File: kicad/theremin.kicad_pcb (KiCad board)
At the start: 2 copper layers, 146 x 91 mm, 47 parts, among them J1 Eurorack Mono Jack, J3 Expression Attachment, SW1 SW_SPDT, U1 4069, U2 4069, U3 LM386, U4 LP2950-5.0_TO92

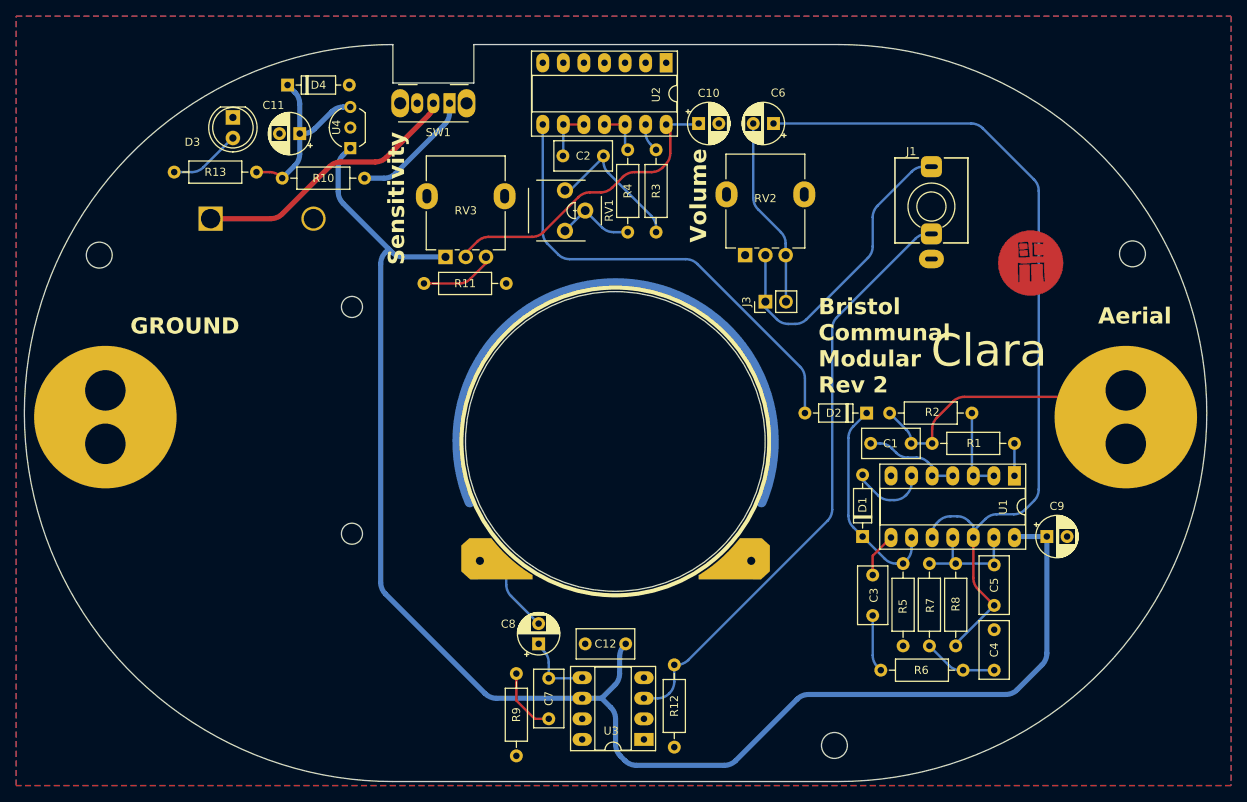
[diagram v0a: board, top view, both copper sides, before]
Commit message: Final tweaks to make sure the front plate holes are on grid
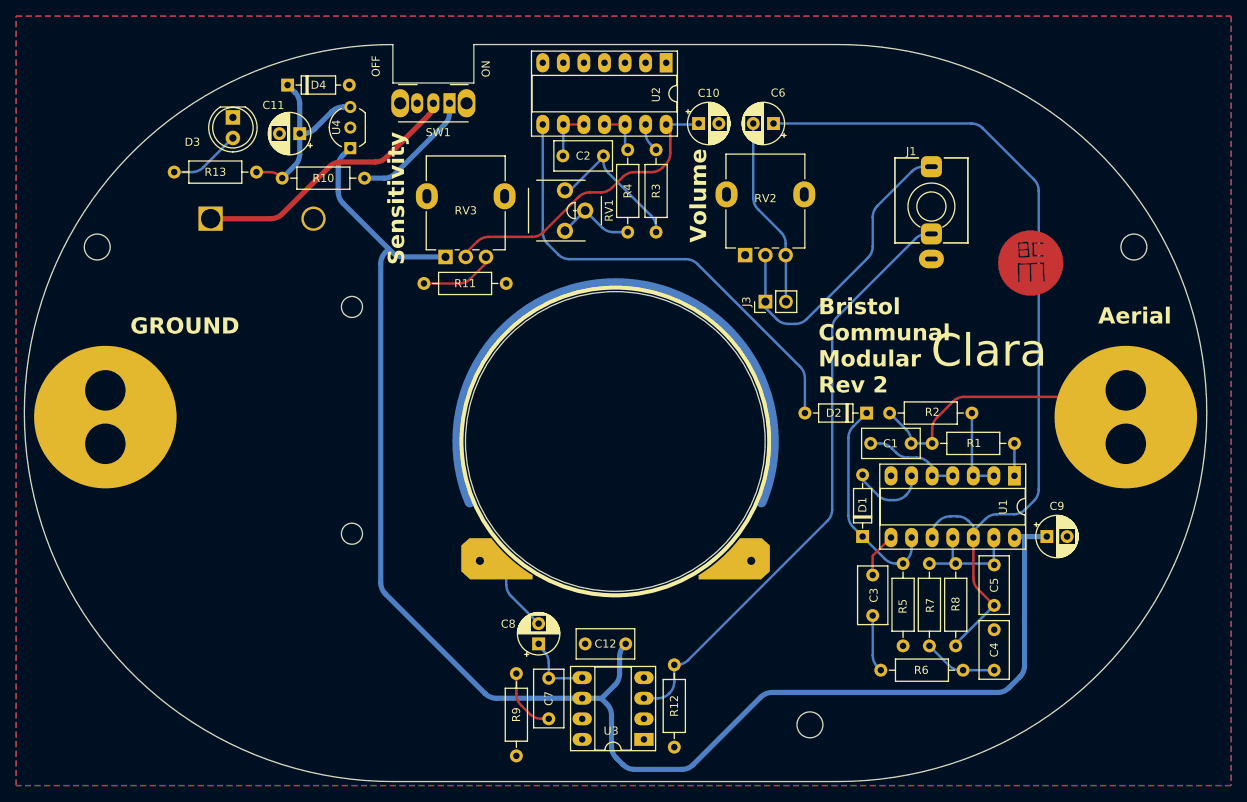
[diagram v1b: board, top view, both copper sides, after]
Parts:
- moved EF** 3.95 mm to (174.0, 135.0)
- moved EF** 1.03 mm to (86.0, 76.0)
- moved EF** 0.86 mm to (214.0, 76.0)
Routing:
- net VCC: track 190.8 -> 189.8 mm
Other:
- board text added: "OFF"
- board text added: "ON"
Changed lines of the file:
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@@
 	(footprint "MountingHole:MountingHole_3.2mm_M3"
 		(layer "F.Cu")
-		(at 86.25 77)
+		(at 86 76)
 		(descr "Mounting Hole 3.2mm, no annular, M3")
 		(tags "mounting hole 3.2mm no annular m3")
@@
 	(footprint "MountingHole:MountingHole_3.2mm_M3"
 		(layer "F.Cu")
-		(at 177.024 137.5454)
+		(at 174 135)
 		(descr "Mounting Hole 3.2mm, no annular, M3")
 		(tags "mounting hole 3.2mm no annular m3")
@@
 	(footprint "MountingHole:MountingHole_3.2mm_M3"
 		(layer "F.Cu")
-		(at 213.824 76.8454)
+		(at 214 76)
 		(descr "Mounting Hole 3.2mm, no annular, M3")
 		(tags "mounting hole 3.2mm no annular m3")
@@
 		)
 	)
+	(gr_text "ON"
+		(at 134 54 90)
+		(layer "F.SilkS")
+		(effects
+			(font
+				(size 1 1)
+				(thickness 0.15)
+			)
+		)
+	)
+	(gr_text "OFF"
+		(at 121 55 90)
+		(layer "F.SilkS")
+		(effects
+			(font
+				(size 1 1)
+				(thickness 0.15)
+			)
+			(justify left bottom)
+		)
+	)
 	(gr_text "Clara"
 		(at 188.94 91.14 0)
@@
 	(segment
 		(start 137.75 128.67)
-		(end 137.75 132)
+		(end 137.75 131.171573)
 		(width 0.3048)
 		(layer "F.Cu")
@@
 	)
 	(segment
-		(start 137.75 132)
-		(end 140 134.25)
+		(start 138.335787 132.585787)
+		(end 139.414214 133.664214)
 		(width 0.3048)
 		(layer "F.Cu")
@@
 	)
 	(segment
-		(start 140 134.25)
+		(start 140.828427 134.25)
 		(end 141.75 134.25)
 		(width 0.3048)
@@
 		(net 11)
 	)
+	(arc
+		(start 137.75 131.171573)
+		(mid 137.902241 131.93694)
+		(end 138.335787 132.585787)
+		(width 0.3048)
+		(layer "F.Cu")
+		(net 11)
+	)
+	(arc
+		(start 139.414214 133.664214)
+		(mid 140.06306 134.097759)
+		(end 140.828427 134.25)
+		(width 0.3048)
+		(layer "F.Cu")
+		(net 11)
+	)
 	(segment
 		(start 140.5 125.25)
@@
 	)
 	(segment
+		(start 152.328427 140.5)
+		(end 158.171573 140.5)
+		(width 0.635)
+		(layer "B.Cu")
+		(net 14)
+	)
+	(segment
 		(start 121.585787 76.664213)
 		(end 122 76.25)
@@
 	)
 	(segment
-		(start 203.25 126.171573)
-		(end 203.25 111.75)
+		(start 148.28 131.78)
+		(end 148.914214 132.414214)
 		(width 0.635)
 		(layer "B.Cu")
@@
 	)
 	(segment
-		(start 115.75 66.078427)
-		(end 115.75 69.171573)
+		(start 200.5 111.75)
+		(end 199.37 111.75)
 		(width 0.635)
 		(layer "B.Cu")
@@
 	)
 	(segment
-		(start 151.085787 125.164213)
-		(end 151.25 125)
+		(start 148.28 131.72)
+		(end 148.28 131.78)
 		(width 0.635)
 		(layer "B.Cu")
@@
 	)
 	(segment
-		(start 117.25 63.79)
-		(end 117.21 63.79)
+		(start 203.25 111.75)
+		(end 200.5 111.75)
 		(width 0.635)
 		(layer "B.Cu")
@@
 	)
 	(segment
-		(start 148.28 131.72)
-		(end 149.914214 130.085786)
+		(start 149.5 133.828427)
+		(end 149.5 137.671573)
 		(width 0.635)
 		(layer "B.Cu")
@@
 	)
 	(segment
-		(start 150.5 128.671573)
-		(end 150.5 126.578427)
+		(start 169.328427 131)
+		(end 197.171573 131)
 		(width 0.635)
 		(layer "B.Cu")
@@
 	)
 	(segment
-		(start 173.828427 131.25)
-		(end 198.171573 131.25)
+		(start 115.75 66.078427)
+		(end 115.75 69.171573)
 		(width 0.635)
 		(layer "B.Cu")
@@
 	)
 	(segment
-		(start 150.585787 138.835787)
-		(end 151.164214 139.414214)
+		(start 151.085787 125.164213)
+		(end 151.25 125)
 		(width 0.635)
 		(layer "B.Cu")
@@
 	)
 	(segment
-		(start 199.37 111.75)
-		(end 199.25 111.87)
+		(start 117.25 63.79)
+		(end 117.21 63.79)
 		(width 0.635)
 		(layer "B.Cu")
@@
 	)
 	(segment
-		(start 199.585787 130.664213)
-		(end 202.664214 127.585786)
+		(start 148.28 131.72)
+		(end 149.914214 130.085786)
 		(width 0.635)
 		(layer "B.Cu")
@@
 	)
 	(segment
-		(start 164.835787 139.414213)
-		(end 172.414214 131.835786)
+		(start 150.085787 139.085787)
+		(end 150.914214 139.914214)
 		(width 0.635)
 		(layer "B.Cu")
@@
 	)
 	(segment
-		(start 150 134.268427)
-		(end 150 137.421573)
+		(start 150.5 128.671573)
+		(end 150.5 126.578427)
 		(width 0.635)
 		(layer "B.Cu")
@@
 	)
 	(segment
-		(start 122 76.25)
-		(end 122.389214 76.639214)
+		(start 199.37 111.75)
+		(end 199.25 111.87)
 		(width 0.635)
 		(layer "B.Cu")
@@
 	)
 	(segment
-		(start 148.28 131.72)
-		(end 149.414214 132.854214)
+		(start 122 76.25)
+		(end 122.389214 76.639214)
 		(width 0.635)
 		(layer "B.Cu")
@@
 	)
 	(segment
+		(start 198.585787 130.414213)
+		(end 199.914214 129.085786)
+		(width 0.635)
+		(layer "B.Cu")
+		(net 14)
+	)
+	(segment
+		(start 200.5 127.671573)
+		(end 200.5 111.75)
+		(width 0.635)
+		(layer "B.Cu")
+		(net 14)
+	)
+	(segment
 		(start 121 78.078427)
 		(end 121 117.421573)
@@
 	)
 	(segment
-		(start 203.25 111.75)
-		(end 199.37 111.75)
+		(start 116.335787 70.585787)
+		(end 122 76.25)
 		(width 0.635)
 		(layer "B.Cu")
@@
 	)
 	(segment
-		(start 116.335787 70.585787)
-		(end 122 76.25)
+		(start 159.585787 139.914213)
+		(end 167.914214 131.585786)
 		(width 0.635)
 		(layer "B.Cu")
 		(net 14)
 	)
-	(segment
-		(start 152.578427 140)
-		(end 163.421573 140)
+	(arc
+		(start 149.5 137.671573)
+		(mid 149.652241 138.43694)
+		(end 150.085787 139.085787)
 		(width 0.635)
 		(layer "B.Cu")
@@
 	)
 	(arc
+		(start 152.328427 140.5)
+		(mid 151.56306 140.347759)
+		(end 150.914214 139.914214)
+		(width 0.635)
+		(layer "B.Cu")
+		(net 14)
+	)
+	(arc
 		(start 121 78.078427)
 		(mid 121.152241 77.31306)
@@
 	)
 	(arc
-		(start 198.171573 131.25)
-		(mid 198.93694 131.097759)
-		(end 199.585787 130.664213)
+		(start 149.5 133.828427)
+		(mid 149.347759 133.06306)
+		(end 148.914214 132.414214)
 		(width 0.635)
 		(layer "B.Cu")
@@
 	)
 	(arc
-		(start 202.664214 127.585786)
-		(mid 203.097759 126.93694)
-		(end 203.25 126.171573)
+		(start 167.914214 131.585786)
+		(mid 168.56306 131.152241)
+		(end 169.328427 131)
 		(width 0.635)
 		(layer "B.Cu")
@@
 	)
 	(arc
-		(start 173.828427 131.25)
-		(mid 173.06306 131.402241)
-		(end 172.414214 131.835786)
-		(width 0.635)
-		(layer "B.Cu")
-		(net 14)
-	)
-	(arc
-		(start 152.578427 140)
-		(mid 151.81306 139.847759)
-		(end 151.164214 139.414214)
+		(start 159.585787 139.914213)
+		(mid 158.93694 140.347759)
+		(end 158.171573 140.5)
 		(width 0.635)
 		(layer "B.Cu")
@@
 	)
 	(arc
-		(start 150 137.421573)
-		(mid 150.152241 138.18694)
-		(end 150.585787 138.835787)
+		(start 200.5 127.671573)
+		(mid 200.347759 128.43694)
+		(end 199.914214 129.085786)
 		(width 0.635)
 		(layer "B.Cu")
@@
 	)
 	(arc
-		(start 150 134.268427)
-		(mid 149.847759 133.50306)
-		(end 149.414214 132.854214)
-		(width 0.635)
-		(layer "B.Cu")
-		(net 14)
-	)
-	(arc
-		(start 163.421573 140)
-		(mid 164.18694 139.847759)
-		(end 164.835787 139.414213)
+		(start 133.884214 131.134214)
+		(mid 134.53306 131.567759)
+		(end 135.298427 131.72)
 		(width 0.635)
 		(layer "B.Cu")
@@
 	)
 	(arc
-		(start 133.884214 131.134214)
-		(mid 134.53306 131.567759)
-		(end 135.298427 131.72)
+		(start 197.171573 131)
+		(mid 197.93694 130.847759)
+		(end 198.585787 130.414213)
 		(width 0.635)
 		(layer "B.Cu")

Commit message: Fixing issues with layout
* Making sure speaker fixing copper isn't covered on speaker footprint
* Adding two more plated holes to make fixing speaker easier
* Making holes for battery holder smaller so easier to solder
* Adding another mounting hole for faceplate
* Tweaking value and reference text placements
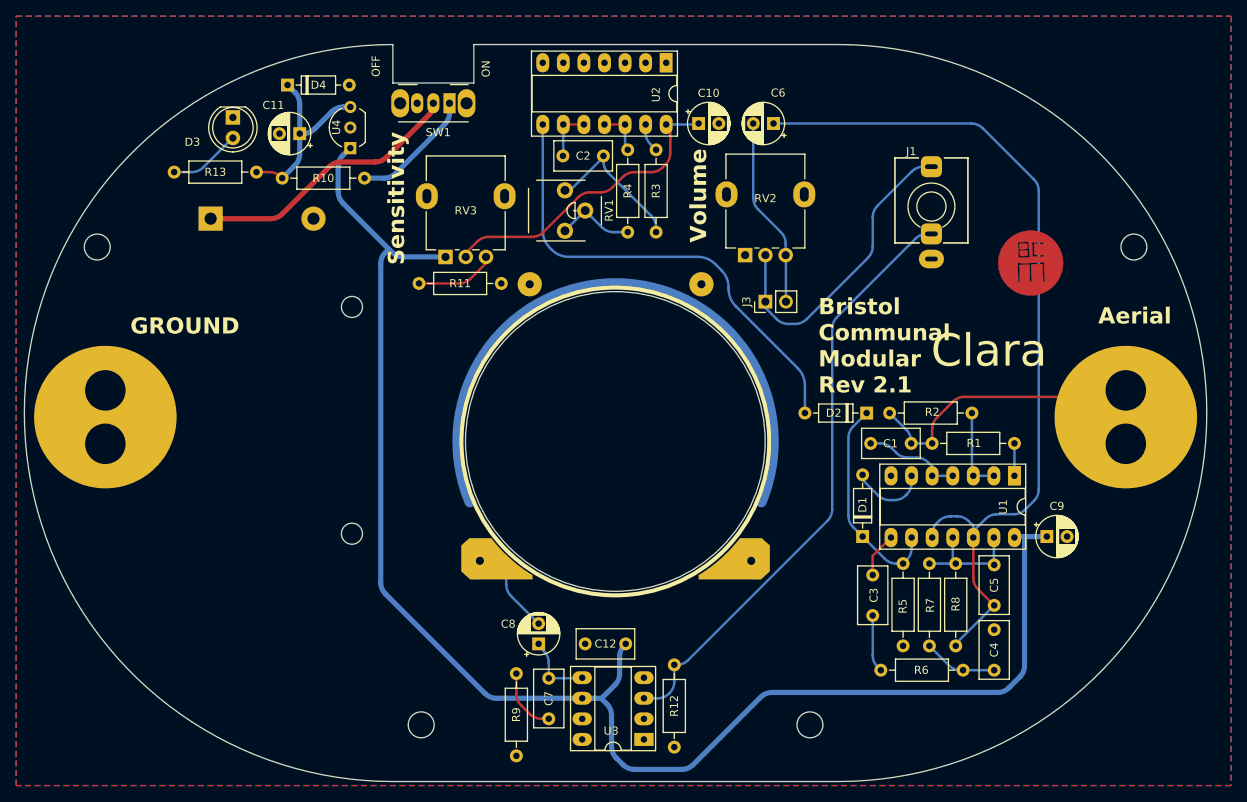
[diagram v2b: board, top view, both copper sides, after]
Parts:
- added EF**: MountingHole_3.2mm_M3, MountingHole:MountingHole_3.2mm_M3, F.Cu at (126.0, 135.0)
- RV1: footprint project-footprints:Potentiometer_THT_Bourns_3306P_Vertical -> Rumblesan_Potentiometer_THT:Potentiometer_THT_Bourns_3306P_Vertical
- moved R11 0.61 mm to (135.9, 80.5)
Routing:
- net Net-(D2-A): track 58.0 -> 59.0 mm
- net Net-(R11-Pad2): track 9.32 -> 9.98 mm
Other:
- board text added: "Bristol Communal Modular Rev 2.1"
- board text removed: "Bristol Communal Modular Rev 2"

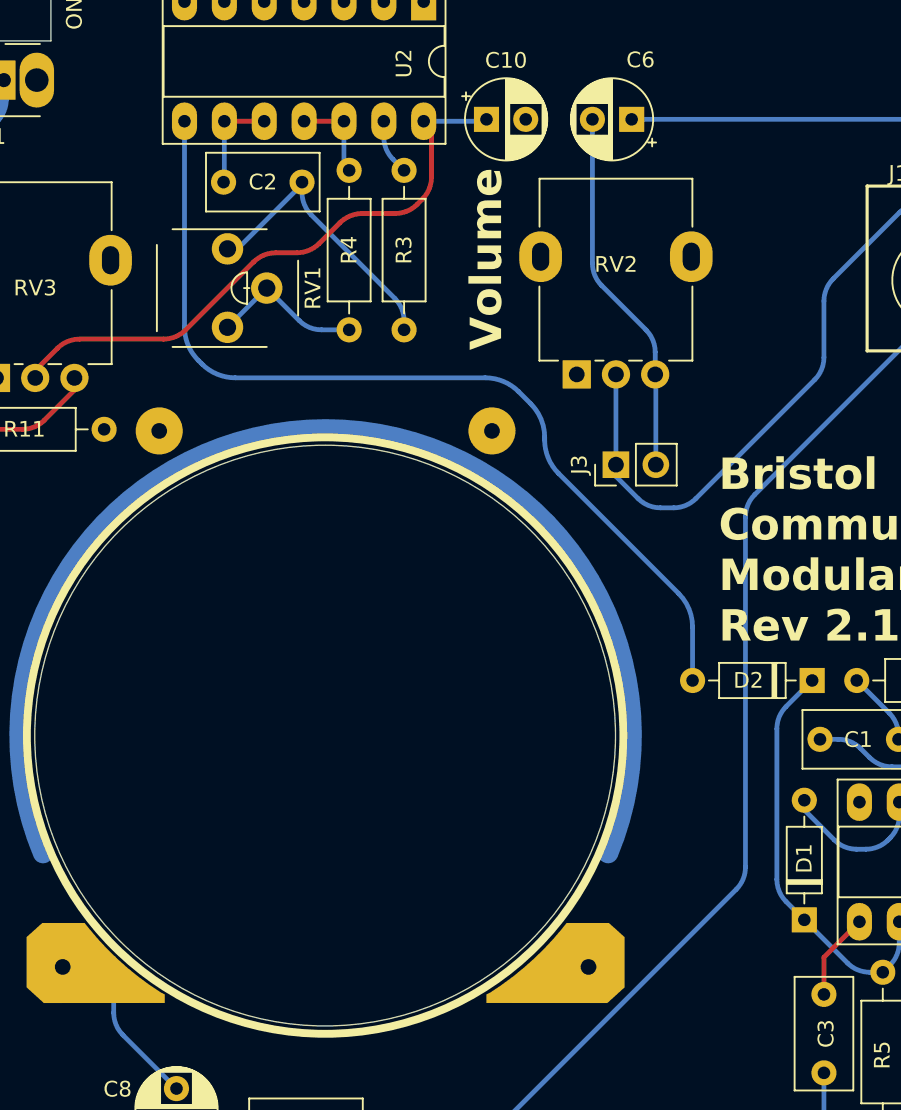
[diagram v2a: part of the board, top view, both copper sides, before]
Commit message: Adding testpoints at output of oscillators
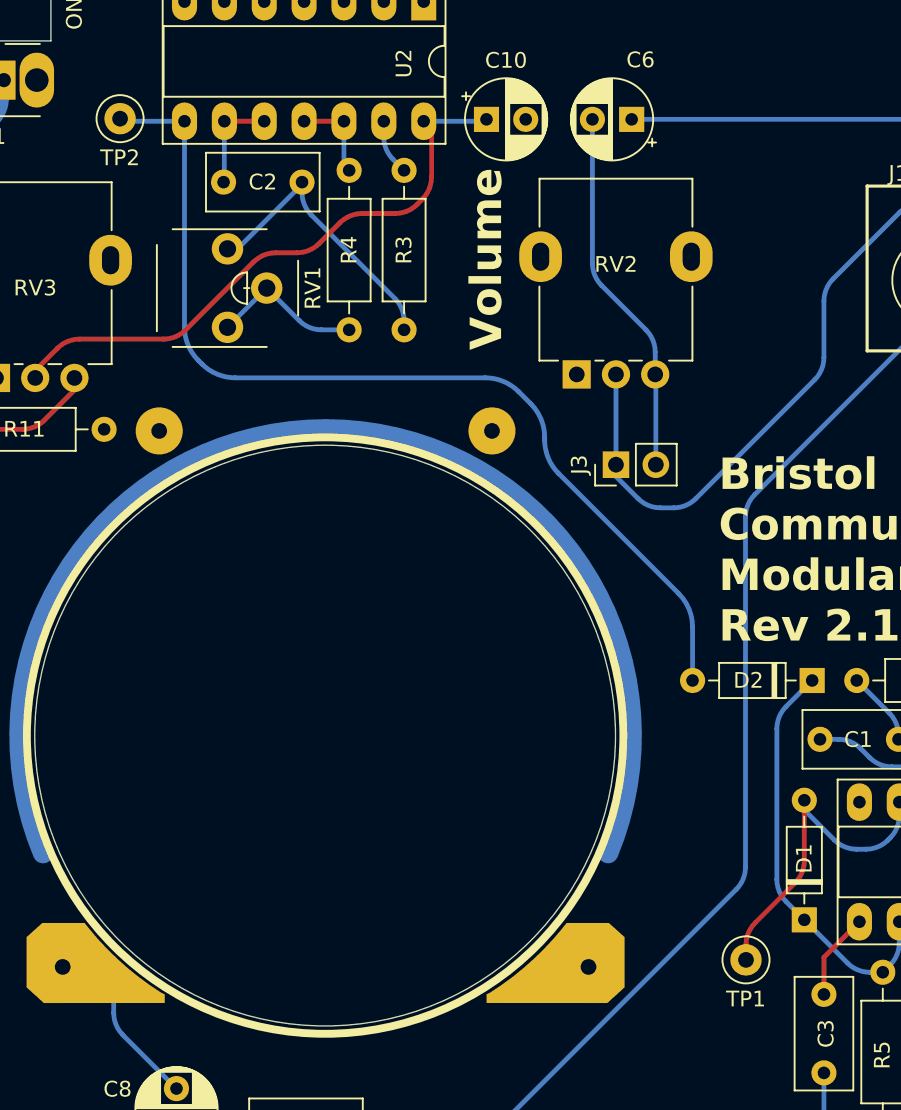
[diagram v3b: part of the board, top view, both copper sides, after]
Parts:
- added TP1: TestPoint, Rumblesan_Standard_Parts:TestPoint_Loop_D2.50mm_Drill1.0mm_LowProfile, F.Cu at (176.8, 114.3)
- added TP2: TestPoint, Rumblesan_Standard_Parts:TestPoint_Loop_D2.50mm_Drill1.0mm_LowProfile, F.Cu at (136.9, 60.7)
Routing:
- net Net-(D1-A): track 9.66 -> 21.2 mm
- net Net-(D2-A): track 59.0 -> 63.1 mm

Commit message: Updating correct LED resistor value
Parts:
- R13: value 1k -> 10k
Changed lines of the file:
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@@
 			)
 		)
-		(property "Value" "1k"
+		(property "Value" "10k"
 			(at 2.75 -0.5 0)
 			(layer "F.Fab")
